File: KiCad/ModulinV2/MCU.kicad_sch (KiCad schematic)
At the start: 1 part, among them IC1 STM32F401VET6

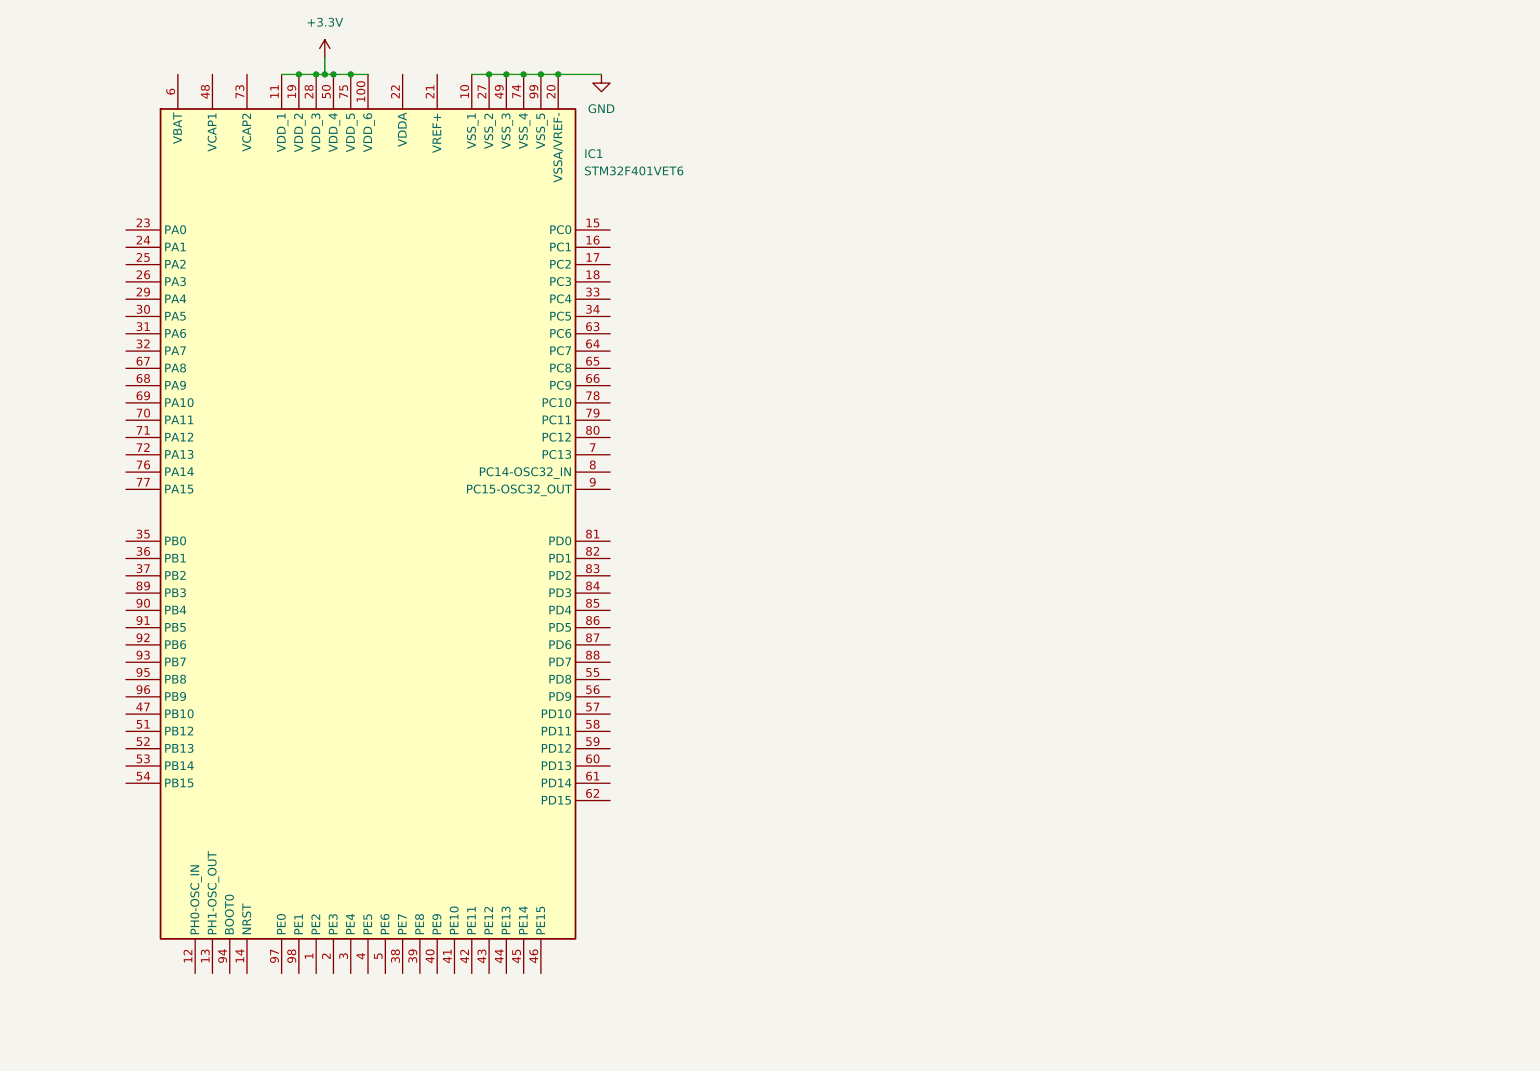
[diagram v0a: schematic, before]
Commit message: Added initial schematic and components for interface
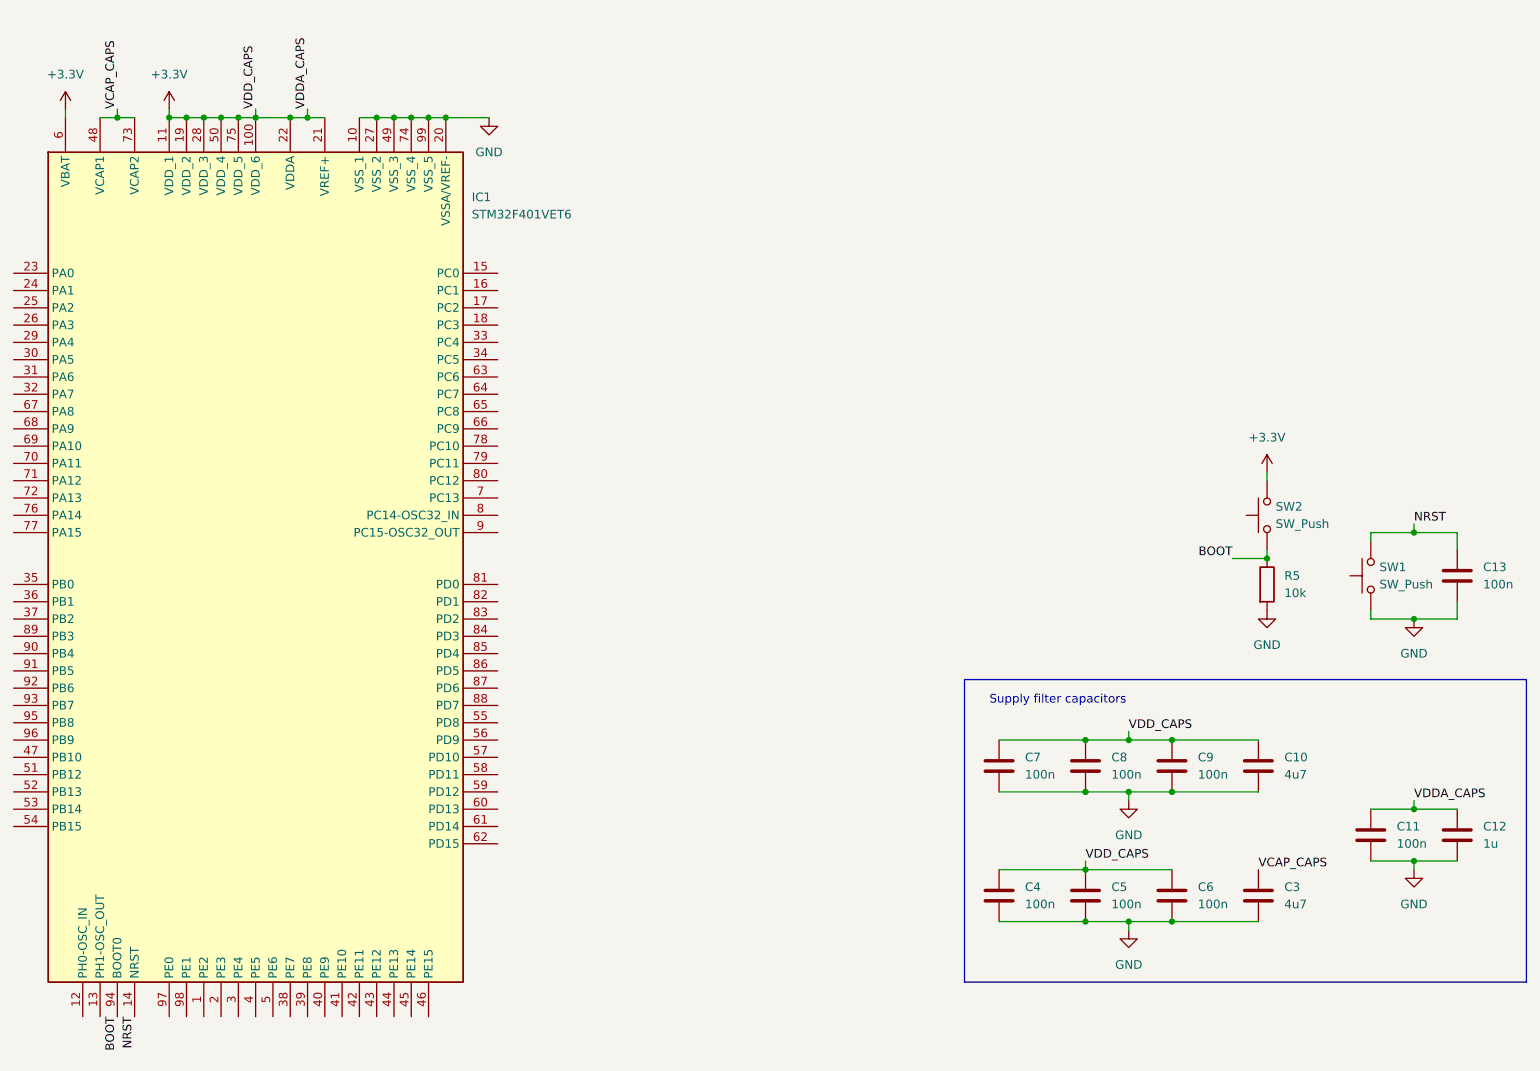
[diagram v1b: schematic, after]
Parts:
- added C10, C3: 4u7, symbol Device:C
- added C11, C13, C4, C5, C6, C7, C8, C9: 100n, symbol Device:C
- added C12: 1u, symbol Device:C
- added R5: 10k, symbol Device:R
- added SW1, SW2: SW_Push, symbol Switch:SW_Push
- IC1: footprint QFP50P1600X1600X160-100N -> Modulin:QFP50P1600X1600X160-100N
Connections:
- net +3.3V: now also IC1.21 (VREF+), IC1.22 (VDDA), IC1.6 (VBAT), C10.1, C11.1, C12.1, C4.1, C5.1, C6.1, C7.1, C8.1, C9.1, SW2.2
- net GND: now also C10.2, C11.2, C12.2, C13.2, C3.2, C4.2, C5.2, C6.2, C7.2, C8.2, C9.2, R5.2, SW1.1
- net NRST: now reaches IC1.14 (NRST)
- net NRST: now also C13.1, SW1.2
- net VCAP_CAPS: now reaches IC1.48 (VCAP1)
- net VCAP_CAPS: now also IC1.73 (VCAP2), C3.1
- net BOOT: now reaches IC1.94 (BOOT0)
- net BOOT: now also R5.1, SW2.1
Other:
- note added: "Supply filter capacitors"
- moved on the sheet: IC1

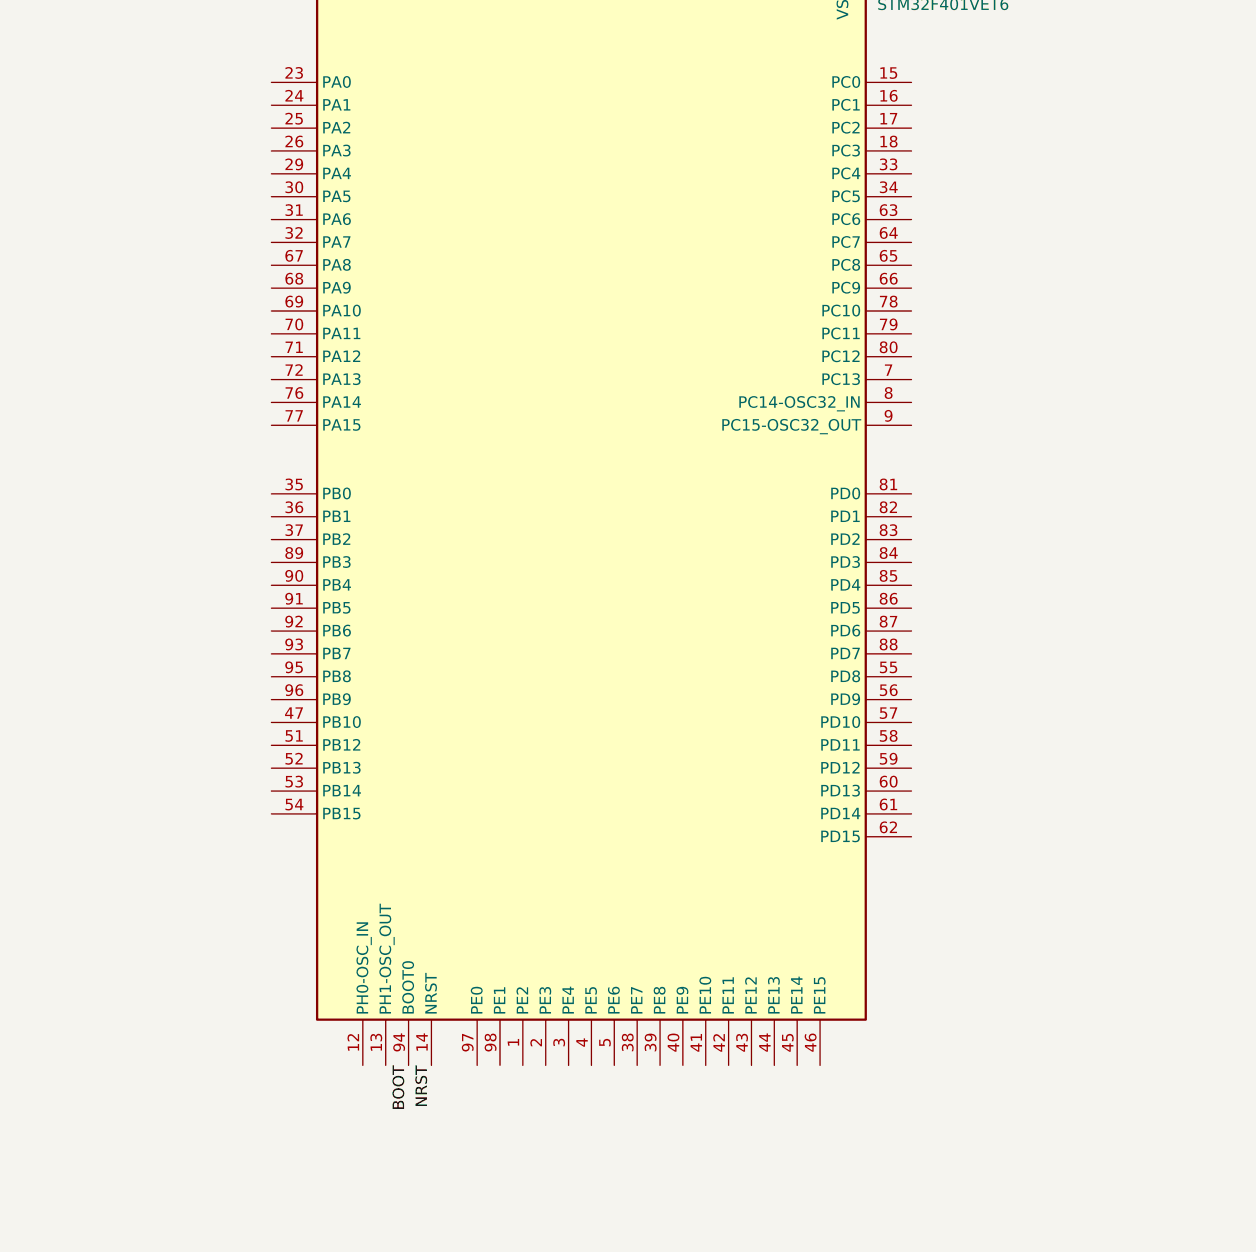
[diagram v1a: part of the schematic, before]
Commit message: Added CubeIDE folder and mapped out initial SPI pins
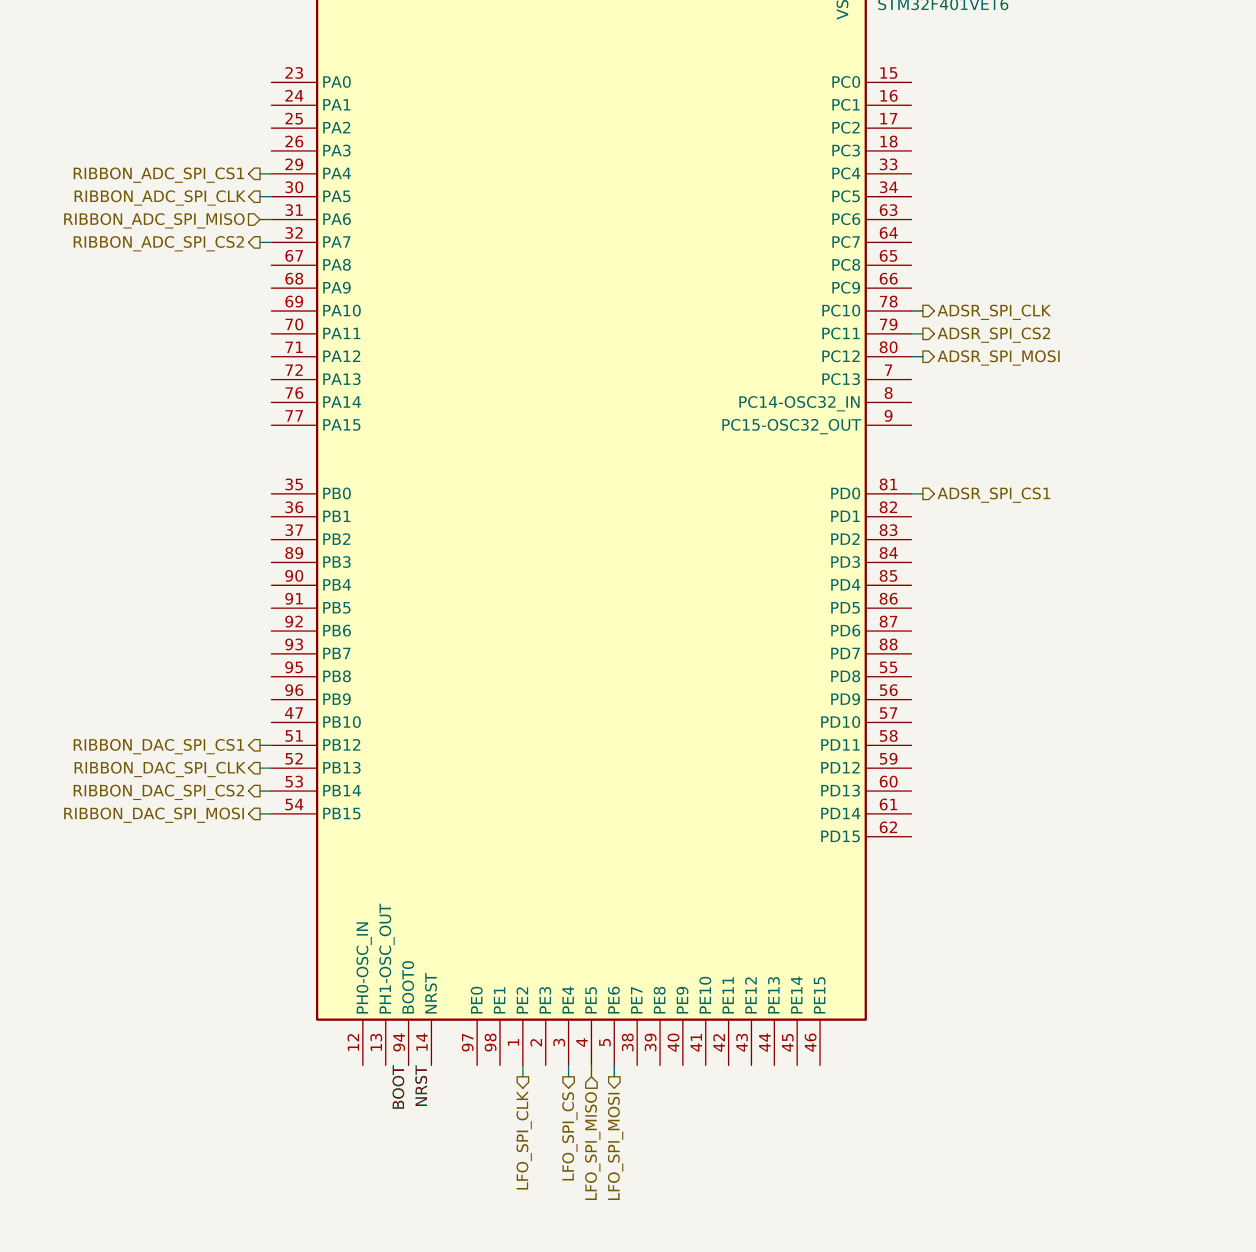
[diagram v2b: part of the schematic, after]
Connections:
- net LFO_SPI_CLK: now reaches IC1.1 (PE2)
- net RIBBON_ADC_SPI_CS1: now reaches IC1.29 (PA4)
- net LFO_SPI_CS: now reaches IC1.3 (PE4)
- net RIBBON_ADC_SPI_CLK: now reaches IC1.30 (PA5)
- net RIBBON_ADC_SPI_MISO: now reaches IC1.31 (PA6)
- net RIBBON_ADC_SPI_CS2: now reaches IC1.32 (PA7)
- net LFO_SPI_MISO: now reaches IC1.4 (PE5)
- net LFO_SPI_MOSI: now reaches IC1.5 (PE6)
- net RIBBON_DAC_SPI_CS1: now reaches IC1.51 (PB12)
- net RIBBON_DAC_SPI_CLK: now reaches IC1.52 (PB13)
- net RIBBON_DAC_SPI_CS2: now reaches IC1.53 (PB14)
- net RIBBON_DAC_SPI_MOSI: now reaches IC1.54 (PB15)
- net ADSR_SPI_CLK: now reaches IC1.78 (PC10)
- net ADSR_SPI_CS2: now reaches IC1.79 (PC11)
- net ADSR_SPI_MOSI: now reaches IC1.80 (PC12)
- net ADSR_SPI_CS1: now reaches IC1.81 (PD0)
